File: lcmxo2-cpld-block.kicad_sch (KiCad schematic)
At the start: 26 parts, among them J12 PMOD, J13 Raspberry_Pi_2_3, U9 LCMXO2-1200HC-4TG100I

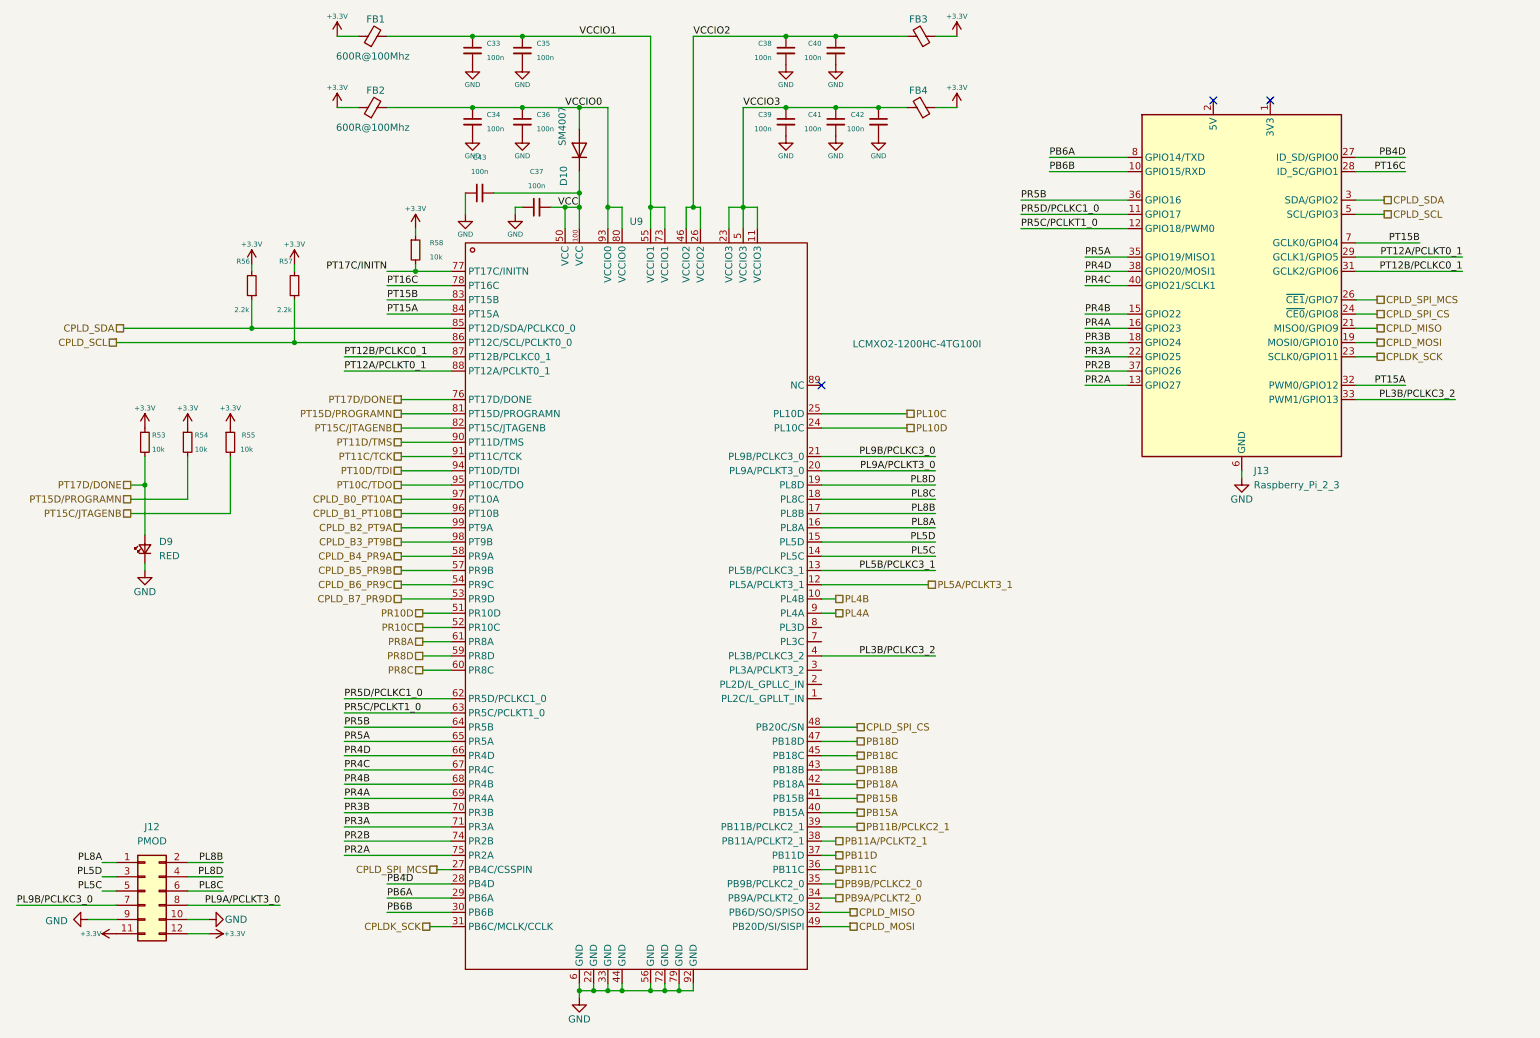
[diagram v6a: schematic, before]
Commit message: Update the footprints
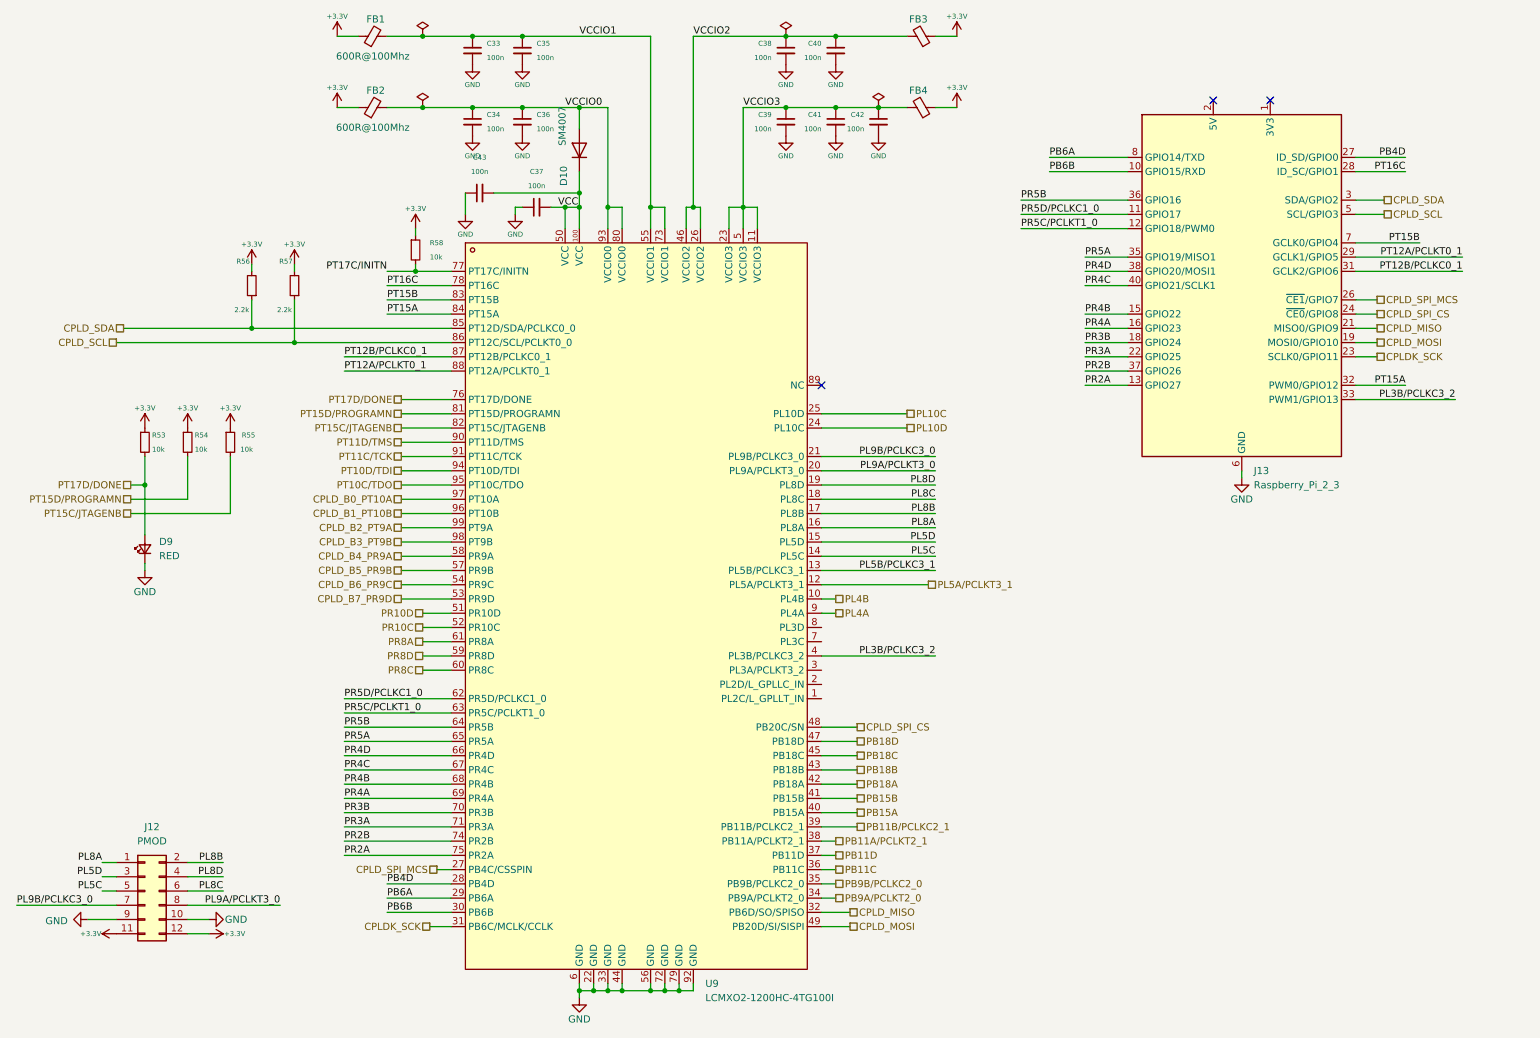
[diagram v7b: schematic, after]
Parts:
- removed U9: LCMXO2-1200HC-4TG100I, Package_QFP:TQFP-100_14x14mm_P0.5mm, symbol EasyEDA_Lib:LCMXO2-1200HC-4TG100I
- added U9: LCMXO2-1200HC-4TG100I, Package_QFP:TQFP-100_14x14mm_P0.5mm, symbol KiCadLocal:LCMXO2-1200HC-4TG100I
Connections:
- net CPLDK_SCK: now also U9.31 (PB6C/MCLK/CCLK)
- net CPLD_B0_PT10A: now also U9.97 (PT10A)
- net CPLD_B1_PT10B: now also U9.96 (PT10B)
- net CPLD_B2_PT9A: now also U9.99 (PT9A)
- net CPLD_B3_PT9B: now also U9.98 (PT9B)
- net CPLD_B4_PR9A: now also U9.58 (PR9A)
- net CPLD_B5_PR9B: now also U9.57 (PR9B)
- net CPLD_B6_PR9C: now also U9.54 (PR9C)
- net CPLD_B7_PR9D: now also U9.53 (PR9D)
- net CPLD_MISO: now also U9.32 (PB6D/SO/SPISO)
- net CPLD_MOSI: now also U9.49 (PB20D/SI/SISPI)
- net CPLD_SCL: now also U9.86 (PT12C/SCL/PCLKT0_0)
- net CPLD_SDA: now also U9.85 (PT12D/SDA/PCLKC0_0)
- net CPLD_SPI_CS: now also U9.48 (PB20C/SN)
- net CPLD_SPI_MCS: now also U9.27 (PB4C/CSSPIN)
- net GND: now also U9.22 (GND), U9.33 (GND), U9.44 (GND), U9.56 (GND), U9.6 (GND), U9.72 (GND), U9.79 (GND), U9.92 (GND)
- net PB11A/PCLKT2_1: now also U9.38 (PB11A/PCLKT2_1)
- net PB11B/PCLKC2_1: now also U9.39 (PB11B/PCLKC2_1)
- net PB11C: now also U9.36 (PB11C)
- net PB11D: now also U9.37 (PB11D)
- net PB15A: now also U9.40 (PB15A)
- net PB15B: now also U9.41 (PB15B)
- net PB18A: now also U9.42 (PB18A)
- net PB18B: now also U9.43 (PB18B)
- net PB18C: now also U9.45 (PB18C)
- net PB18D: now also U9.47 (PB18D)
- net PB4D: now also U9.28 (PB4D)
- net PB6A: now also U9.29 (PB6A)
- net PB6B: now also U9.30 (PB6B)
- net PB9A/PCLKT2_0: now also U9.34 (PB9A/PCLKT2_0)
- net PB9B/PCLKC2_0: now also U9.35 (PB9B/PCLKC2_0)
- net PL10C: now also U9.25 (PL10D)
- net PL10D: now also U9.24 (PL10C)
- net PL3B/PCLKC3_2: now also U9.4 (PL3B/PCLKC3_2)
- net PL4A: now also U9.9 (PL4A)
- net PL4B: now also U9.10 (PL4B)
- net PL5A/PCLKT3_1: now also U9.12 (PL5A/PCLKT3_1)
- net PL5B/PCLKC3_1: now also U9.13 (PL5B/PCLKC3_1)
- net PL5C: now also U9.14 (PL5C)
- net PL5D: now also U9.15 (PL5D)
- net PL8A: now also U9.16 (PL8A)
- net PL8B: now also U9.17 (PL8B)
- net PL8C: now also U9.18 (PL8C)
- net PL8D: now also U9.19 (PL8D)
- net PL9A/PCLKT3_0: now also U9.20 (PL9A/PCLKT3_0)
- net PL9B/PCLKC3_0: now also U9.21 (PL9B/PCLKC3_0)
- net PR10C: now also U9.52 (PR10C)
- net PR10D: now also U9.51 (PR10D)
- net PR2A: now also U9.75 (PR2A)
- net PR2B: now also U9.74 (PR2B)
- net PR3A: now also U9.71 (PR3A)
- net PR3B: now also U9.70 (PR3B)
- net PR4A: now also U9.69 (PR4A)
- net PR4B: now also U9.68 (PR4B)
- net PR4C: now also U9.67 (PR4C)
- net PR4D: now also U9.66 (PR4D)
- net PR5A: now also U9.65 (PR5A)
- net PR5B: now also U9.64 (PR5B)
- net PR5C/PCLKT1_0: now also U9.63 (PR5C/PCLKT1_0)
- net PR5D/PCLKC1_0: now also U9.62 (PR5D/PCLKC1_0)
- net PR8A: now also U9.61 (PR8A)
- net PR8C: now also U9.60 (PR8C)
- net PR8D: now also U9.59 (PR8D)
- net PT10C/TDO: now also U9.95 (PT10C/TDO)
- net PT10D/TDI: now also U9.94 (PT10D/TDI)
- net PT11C/TCK: now also U9.91 (PT11C/TCK)
- net PT11D/TMS: now also U9.90 (PT11D/TMS)
- net PT12A/PCLKT0_1: now also U9.88 (PT12A/PCLKT0_1)
- net PT12B/PCLKC0_1: now also U9.87 (PT12B/PCLKC0_1)
- net PT15A: now also U9.84 (PT15A)
- net PT15B: now also U9.83 (PT15B)
- net PT15C/JTAGENB: now also U9.82 (PT15C/JTAGENB)
- net PT15D/PROGRAMN: now also U9.81 (PT15D/PROGRAMN)
- net PT16C: now also U9.78 (PT16C)
- net PT17C/INITN: now also U9.77 (PT17C/INITN)
- net PT17D/DONE: now also U9.76 (PT17D/DONE)
- net VCC: now also U9.100 (VCC), U9.50 (VCC)
- net VCCIO0: now also U9.80 (VCCIO0), U9.93 (VCCIO0)
- net VCCIO1: now also U9.55 (VCCIO1), U9.73 (VCCIO1)
- net VCCIO2: now also U9.26 (VCCIO2), U9.46 (VCCIO2)
- net VCCIO3: now also U9.11 (VCCIO3), U9.23 (VCCIO3), U9.5 (VCCIO3)

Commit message: Update the BOM and the routing
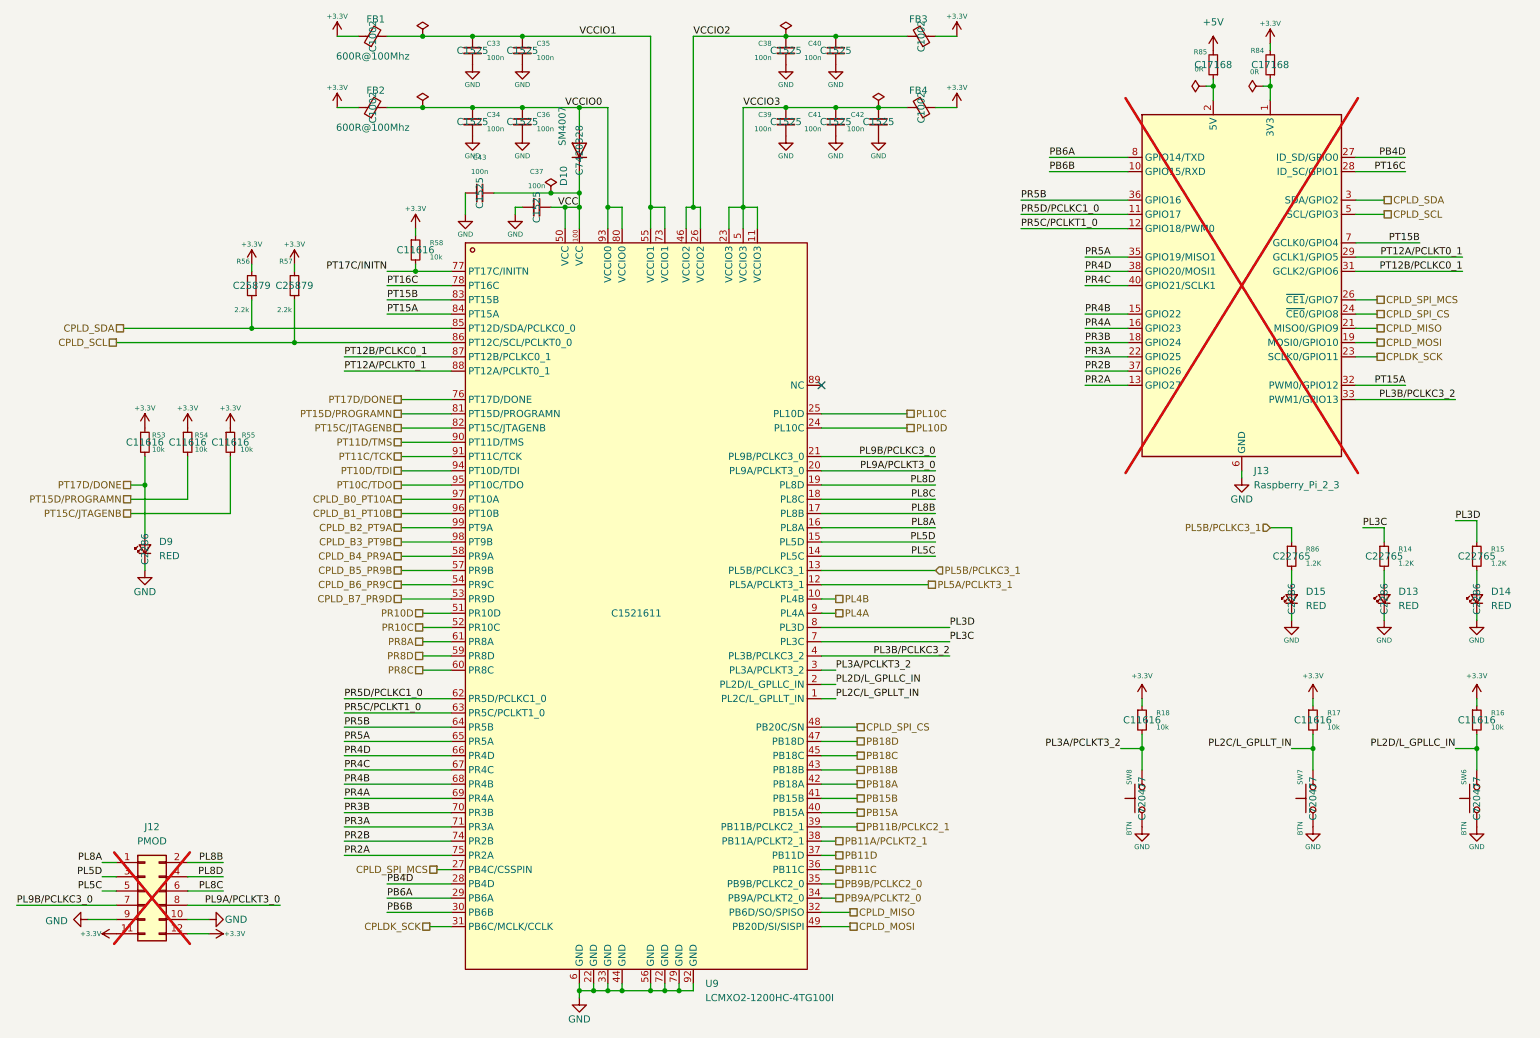
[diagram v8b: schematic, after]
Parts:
- added D13, D14, D15: RED, LED_SMD:LED_0603_1608Metric, symbol Device:LED_Small
- added R14, R15, R86: 1.2K, Resistor_SMD:R_0603_1608Metric, symbol Device:R_Small
- added R16, R17, R18: 10k, Resistor_SMD:R_0402_1005Metric, symbol Device:R_Small
- added R84, R85: 0R, Resistor_SMD:R_0402_1005Metric, symbol Device:R_Small
- added SW6, SW7, SW8: BTN, EasyEDA_Lib:SW-SMD_L3.9-W3.0-P4.45, symbol Switch:SW_Push
- C33, C34, C35, C36, C37, C38, C39, C40, C41, C42, C43: LCSC (none) -> C1525
- D10: LCSC (none) -> C7420328
- D9: LCSC (none) -> C2286
- FB1, FB2, FB3, FB4: LCSC (none) -> C1002
- J12, J13: now not fitted; now left out of the parts list
- R53, R54, R55, R58: LCSC (none) -> C11616
- R56, R57: LCSC (none) -> C25879
- U9: LCSC (none) -> C1521611; Manufacturer Part LCMXO2-1200HC-4TG100I -> (none); Supplier LCSC -> (none); Supplier Part C1521611 -> (none)
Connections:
- net +3.3V: now also R16.1, R17.1, R18.1, R84.2
- net GND: now also D13.1 (K), D14.1 (K), D15.1 (K), SW6.1, SW7.1, SW8.1
- net at J13.1 (3V3), J13.17 (3V3): now also R84.1
- net at J13.2 (5V), J13.4 (5V): now also R85.1
- net PL2C/L_GPLLT_IN: now reaches U9.1 (PL2C/L_GPLLT_IN)
- net PL2C/L_GPLLT_IN: now also R17.2, SW7.2
- net PL2D/L_GPLLC_IN: now reaches U9.2 (PL2D/L_GPLLC_IN)
- net PL2D/L_GPLLC_IN: now also R16.2, SW6.2
- net PL3A/PCLKT3_2: now reaches U9.3 (PL3A/PCLKT3_2)
- net PL3A/PCLKT3_2: now also R18.2, SW8.2
- net PL3C: now reaches U9.7 (PL3C)
- net PL3C: now also R14.1
- net PL3D: now reaches U9.8 (PL3D)
- net PL3D: now also R15.1
- net PL5B/PCLKC3_1 renamed PL5B/PCLKC3_1
- net PL5B/PCLKC3_1: now also R86.1
- new net: D13.2 (A), R14.2
- new net: D15.2 (A), R86.2
- new net: D14.2 (A), R15.2
- new net +5V: R85.2
- no-connect marks 3 -> 1
